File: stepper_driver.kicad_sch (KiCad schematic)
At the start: 7 parts, among them J20 StepperA, J21 StepperB, U3 TMC2208_SILENTSTEPSTICK

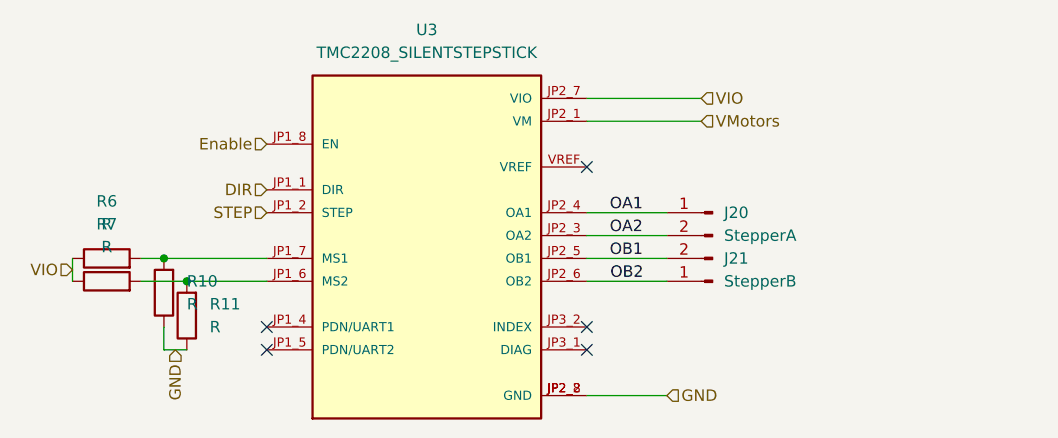
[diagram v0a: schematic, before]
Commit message: add second AX12 connector + change stepper connectors + add 12V connector. Todo : add SPI for RFID
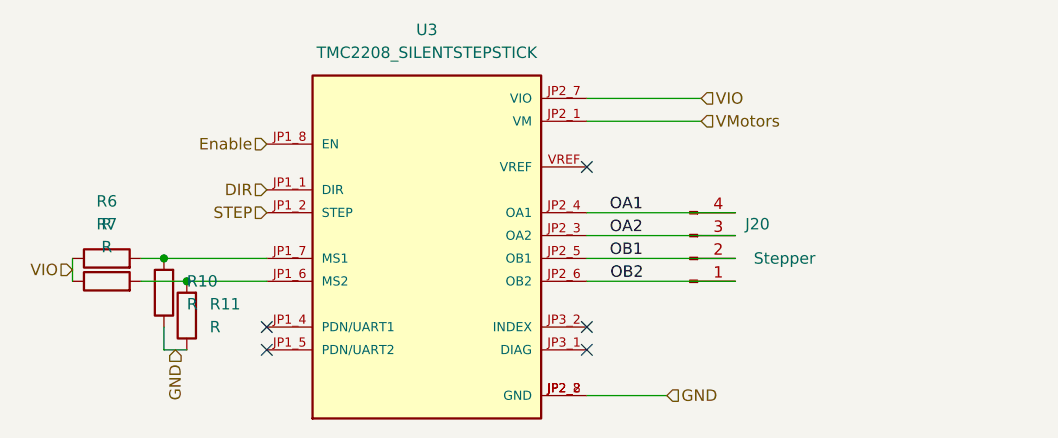
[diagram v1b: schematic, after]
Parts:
- removed J20: StepperA, Connector_Phoenix_MC:PhoenixContact_MC_1,5_2-G-3.81_1x02_P3.81mm_Horizontal, symbol Connector:Conn_01x02_Male
- removed J21: StepperB, Connector_Phoenix_MC:PhoenixContact_MC_1,5_2-G-3.81_1x02_P3.81mm_Horizontal, symbol Connector:Conn_01x02_Male
- added J20: Stepper, Connector_JST:JST_XH_B4B-XH-A_1x04_P2.50mm_Vertical, symbol Connector:Conn_01x04_Male
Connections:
- net OA1: now also J20.4 (Pin_4)
- net OA2: now also J20.3 (Pin_3)
- net OB1: now also J20.2 (Pin_2)
- net OB2: now also J20.1 (Pin_1)
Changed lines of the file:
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@@
   (no_connect (at 92.71 87.63))
   (no_connect (at 128.27 85.09))
-  (wire (pts (xy 137.16 72.39) (xy 128.27 72.39))
+  (wire (pts (xy 144.78 72.39) (xy 128.27 72.39))
     (stroke (width 0) (type default) (color 0 0 0 0))
   )
@@
     (stroke (width 0) (type default) (color 0 0 0 0))
   )
-  (wire (pts (xy 137.16 80.01) (xy 128.27 80.01))
+  (wire (pts (xy 144.78 80.01) (xy 128.27 80.01))
     (stroke (width 0) (type default) (color 0 0 0 0))
   )
@@
     (stroke (width 0) (type default) (color 0 0 0 0))
   )
-  (wire (pts (xy 137.16 77.47) (xy 128.27 77.47))
+  (wire (pts (xy 144.78 77.47) (xy 128.27 77.47))
     (stroke (width 0) (type default) (color 0 0 0 0))
   )
@@
     (stroke (width 0) (type default) (color 0 0 0 0))
   )
-  (wire (pts (xy 137.16 74.93) (xy 128.27 74.93))
+  (wire (pts (xy 144.78 74.93) (xy 128.27 74.93))
     (stroke (width 0) (type default) (color 0 0 0 0))
   )
@@
     (pin "1")
     (pin "2")
+  )
+  (symbol (lib_id "Connector:Conn_01x04_Male") (at 139.7 77.47 0) (mirror x) (unit 1)
+    (in_bom yes) (on_board yes)
+    (property "Reference" "J20" (id 0) (at 148.59 73.66 0)
+      (effects (font (size 1.27 1.27)) (justify right))
+    )
+    (property "Value" "Stepper" (id 1) (at 153.67 77.47 0)
+      (effects (font (size 1.27 1.27)) (justify right))
+    )
+    (property "Footprint" "Connector_JST:JST_XH_B4B-XH-A_1x04_P2.50mm_Vertical" (id 2) (at 139.7 77.47 0)
+      (effects (font (size 1.27 1.27)) hide)
+    )
+    (property "Datasheet" "~" (id 3) (at 139.7 77.47 0)
+      (effects (font (size 1.27 1.27)) hide)
+    )
+    (pin "1")
+    (pin "2")
+    (pin "3")
+    (pin "4")
   )
   (symbol (lib_id "TMC2208_SILENTSTEPSTICK:TMC2208_SILENTSTEPSTICK") (at 110.49 74.93 0) (unit 1)
@@
     (pin "VREF")
   )
-  (symbol (lib_id "Connector:Conn_01x02_Male") (at 142.24 80.01 180) (unit 1)
-    (in_bom yes) (on_board yes) (fields_autoplaced)
-    (property "Reference" "J21" (id 0) (at 143.51 77.4699 0)
-      (effects (font (size 1.27 1.27)) (justify right))
-    )
-    (property "Value" "StepperB" (id 1) (at 143.51 80.0099 0)
-      (effects (font (size 1.27 1.27)) (justify right))
-    )
-    (property "Footprint" "Connector_Phoenix_MC:PhoenixContact_MC_1,5_2-G-3.81_1x02_P3.81mm_Horizontal" (id 2) (at 142.24 80.01 0)
-      (effects (font (size 1.27 1.27)) hide)
-    )
-    (property "Datasheet" "~" (id 3) (at 142.24 80.01 0)
-      (effects (font (size 1.27 1.27)) hide)
-    )
-    (pin "1")
-    (pin "2")
-  )
   (symbol (lib_id "Device:R") (at 81.28 81.28 180) (unit 1)
     (in_bom yes) (on_board yes) (fields_autoplaced)
@@
       (effects (font (size 1.27 1.27)) hide)
     )
-    (pin "1")
-    (pin "2")
-  )
-  (symbol (lib_id "Connector:Conn_01x02_Male") (at 142.24 72.39 0) (mirror y) (unit 1)
-    (in_bom yes) (on_board yes) (fields_autoplaced)
-    (property "Reference" "J20" (id 0) (at 143.51 72.3899 0)
-      (effects (font (size 1.27 1.27)) (justify right))
-    )
-    (property "Value" "StepperA" (id 1) (at 143.51 74.9299 0)
-      (effects (font (size 1.27 1.27)) (justify right))
-    )
-    (property "Footprint" "Connector_Phoenix_MC:PhoenixContact_MC_1,5_2-G-3.81_1x02_P3.81mm_Horizontal" (id 2) (at 142.24 72.39 0)
-      (effects (font (size 1.27 1.27)) hide)
-    )
-    (property "Datasheet" "~" (id 3) (at 142.24 72.39 0)
-      (effects (font (size 1.27 1.27)) hide)
-    )

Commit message: Add SPI connector + route control pins (LEDs, AX12)
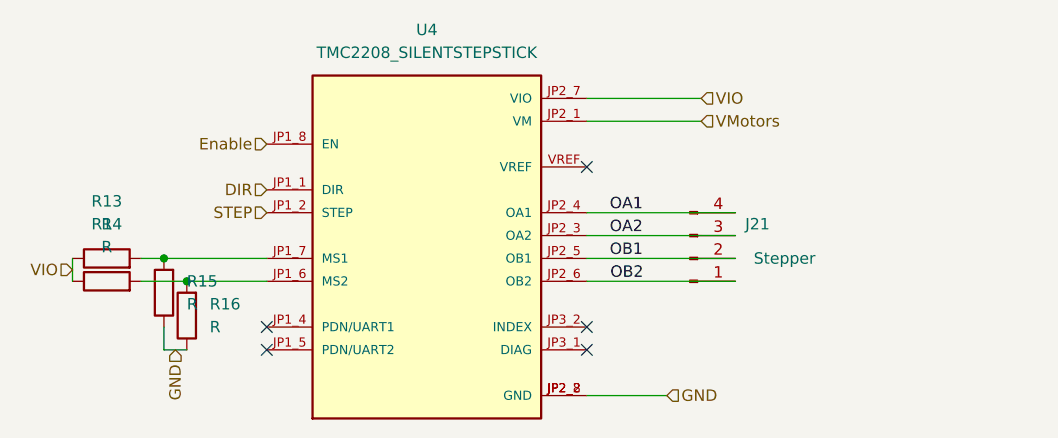
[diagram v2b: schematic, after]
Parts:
- renumbered J20 to J21, R6 to R13, R7 to R14, R10 to R15, R11 to R16, U3 to U4
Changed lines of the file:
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@@
     (effects (font (size 1.27 1.27)) (justify left))
   )
-  (symbol (lib_id "Device:R") (at 74.93 80.01 90) (unit 1)
+  (symbol (lib_id "Device:R") (at 74.93 80.01 90)
     (in_bom yes) (on_board yes) (fields_autoplaced)
-    (property "Reference" "R7" (id 0) (at 74.93 73.66 90))
+    (property "Reference" "R14" (id 0) (at 74.93 73.66 90))
     (property "Value" "R" (id 1) (at 74.93 76.2 90))
     (property "Footprint" "Resistor_SMD:R_0603_1608Metric" (id 2) (at 74.93 81.788 90)
@@
     (pin "2")
   )
-  (symbol (lib_id "Device:R") (at 83.82 83.82 180) (unit 1)
+  (symbol (lib_id "Device:R") (at 83.82 83.82 180)
     (in_bom yes) (on_board yes) (fields_autoplaced)
-    (property "Reference" "R11" (id 0) (at 86.36 82.5499 0)
+    (property "Reference" "R16" (id 0) (at 86.36 82.5499 0)
       (effects (font (size 1.27 1.27)) (justify right))
     )
@@
     (pin "2")
   )
-  (symbol (lib_id "Connector:Conn_01x04_Male") (at 139.7 77.47 0) (mirror x) (unit 1)
+  (symbol (lib_id "Connector:Conn_01x04_Male") (at 139.7 77.47 0) (mirror x)
     (in_bom yes) (on_board yes)
-    (property "Reference" "J20" (id 0) (at 148.59 73.66 0)
+    (property "Reference" "J21" (id 0) (at 148.59 73.66 0)
       (effects (font (size 1.27 1.27)) (justify right))
     )
@@
     (pin "4")
   )
-  (symbol (lib_id "TMC2208_SILENTSTEPSTICK:TMC2208_SILENTSTEPSTICK") (at 110.49 74.93 0) (unit 1)
+  (symbol (lib_id "TMC2208_SILENTSTEPSTICK:TMC2208_SILENTSTEPSTICK") (at 110.49 74.93 0)
     (in_bom yes) (on_board yes) (fields_autoplaced)
-    (property "Reference" "U3" (id 0) (at 110.49 52.07 0))
+    (property "Reference" "U4" (id 0) (at 110.49 52.07 0))
     (property "Value" "TMC2208_SILENTSTEPSTICK" (id 1) (at 110.49 54.61 0))
     (property "Footprint" "TMC2208_SILENTSTEPSTICK:MODULE_TMC2208_SILENTSTEPSTICK" (id 2) (at 110.49 74.93 0)
@@
     (pin "VREF")
   )
-  (symbol (lib_id "Device:R") (at 81.28 81.28 180) (unit 1)
+  (symbol (lib_id "Device:R") (at 81.28 81.28 180)
     (in_bom yes) (on_board yes) (fields_autoplaced)
-    (property "Reference" "R10" (id 0) (at 83.82 80.0099 0)
+    (property "Reference" "R15" (id 0) (at 83.82 80.0099 0)
       (effects (font (size 1.27 1.27)) (justify right))
     )
@@
     (pin "2")
   )
-  (symbol (lib_id "Device:R") (at 74.93 77.47 90) (unit 1)
+  (symbol (lib_id "Device:R") (at 74.93 77.47 90)
     (in_bom yes) (on_board yes) (fields_autoplaced)
-    (property "Reference" "R6" (id 0) (at 74.93 71.12 90))
+    (property "Reference" "R13" (id 0) (at 74.93 71.12 90))
     (property "Value" "R" (id 1) (at 74.93 73.66 90))
     (property "Footprint" "Resistor_SMD:R_0603_1608Metric" (id 2) (at 74.93 79.248 90)

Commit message: add zeners for new connections
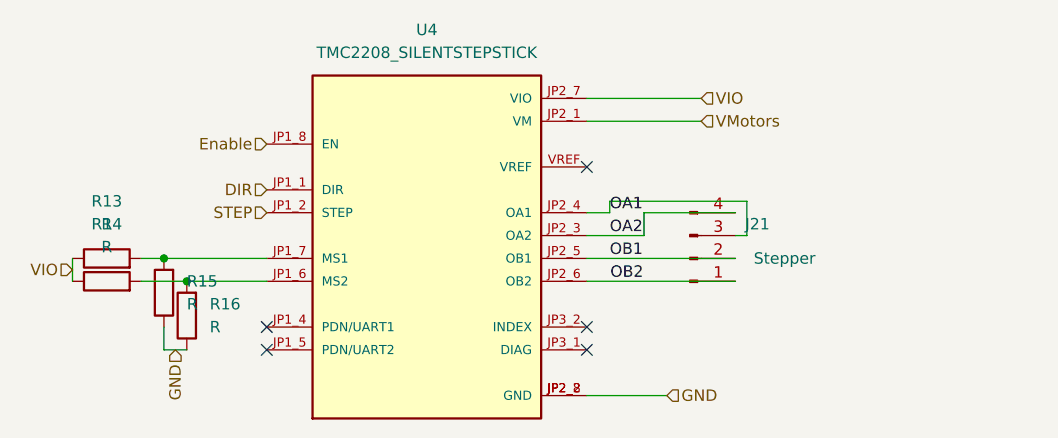
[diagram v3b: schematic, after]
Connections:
- net OA1: now also J21.3 (Pin_3); no longer J21.4 (Pin_4)
- net OA2: now also J21.4 (Pin_4); no longer J21.3 (Pin_3)
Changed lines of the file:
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@@
   (no_connect (at 92.71 87.63))
   (no_connect (at 128.27 85.09))
-  (wire (pts (xy 144.78 72.39) (xy 128.27 72.39))
-    (stroke (width 0) (type default) (color 0 0 0 0))
-  )
   (wire (pts (xy 137.16 92.71) (xy 128.27 92.71))
     (stroke (width 0) (type default) (color 0 0 0 0))
@@
     (stroke (width 0) (type default) (color 0 0 0 0))
   )
+  (wire (pts (xy 128.27 74.93) (xy 134.62 74.93))
+    (stroke (width 0) (type default) (color 0 0 0 0))
+  )
   (wire (pts (xy 78.74 80.01) (xy 83.82 80.01))
+    (stroke (width 0) (type default) (color 0 0 0 0))
+  )
+  (wire (pts (xy 128.27 72.39) (xy 130.81 72.39))
+    (stroke (width 0) (type default) (color 0 0 0 0))
+  )
+  (wire (pts (xy 134.62 72.39) (xy 144.78 72.39))
     (stroke (width 0) (type default) (color 0 0 0 0))
   )
@@
     (stroke (width 0) (type default) (color 0 0 0 0))
   )
+  (wire (pts (xy 146.05 74.93) (xy 144.78 74.93))
+    (stroke (width 0) (type default) (color 0 0 0 0))
+  )
   (wire (pts (xy 81.28 87.63) (xy 81.28 85.09))
+    (stroke (width 0) (type default) (color 0 0 0 0))
+  )
+  (wire (pts (xy 130.81 72.39) (xy 130.81 71.12))
     (stroke (width 0) (type default) (color 0 0 0 0))
   )
@@
     (stroke (width 0) (type default) (color 0 0 0 0))
   )
+  (wire (pts (xy 146.05 71.12) (xy 146.05 74.93))
+    (stroke (width 0) (type default) (color 0 0 0 0))
+  )
+  (wire (pts (xy 134.62 74.93) (xy 134.62 72.39))
+    (stroke (width 0) (type default) (color 0 0 0 0))
+  )
   (wire (pts (xy 81.28 77.47) (xy 92.71 77.47))
     (stroke (width 0) (type default) (color 0 0 0 0))
@@
     (stroke (width 0) (type default) (color 0 0 0 0))
   )
-  (wire (pts (xy 144.78 74.93) (xy 128.27 74.93))
+  (wire (pts (xy 130.81 71.12) (xy 146.05 71.12))
     (stroke (width 0) (type default) (color 0 0 0 0))
   )

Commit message: route STEP and DIR for both stepper motors
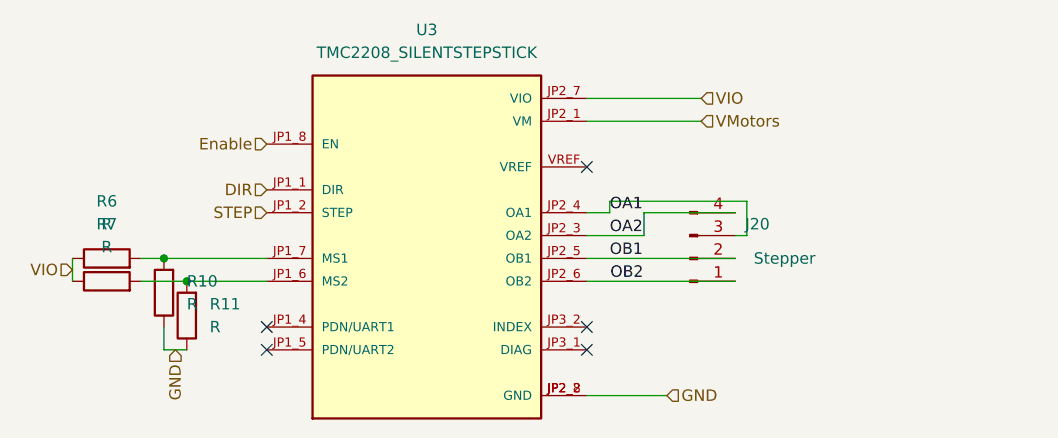
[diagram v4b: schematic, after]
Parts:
- renumbered J21 to J20, R15 to R10, R16 to R11, R13 to R6, R14 to R7, U4 to U3
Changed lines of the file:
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@@
     (effects (font (size 1.27 1.27)) (justify left))
   )
-  (symbol (lib_id "Device:R") (at 74.93 80.01 90)
+  (symbol (lib_id "Device:R") (at 74.93 80.01 90) (unit 1)
     (in_bom yes) (on_board yes) (fields_autoplaced)
-    (property "Reference" "R14" (id 0) (at 74.93 73.66 90))
+    (property "Reference" "R7" (id 0) (at 74.93 73.66 90))
     (property "Value" "R" (id 1) (at 74.93 76.2 90))
     (property "Footprint" "Resistor_SMD:R_0603_1608Metric" (id 2) (at 74.93 81.788 90)
@@
     (pin "2")
   )
-  (symbol (lib_id "Device:R") (at 83.82 83.82 180)
+  (symbol (lib_id "Device:R") (at 83.82 83.82 180) (unit 1)
     (in_bom yes) (on_board yes) (fields_autoplaced)
-    (property "Reference" "R16" (id 0) (at 86.36 82.5499 0)
+    (property "Reference" "R11" (id 0) (at 86.36 82.5499 0)
       (effects (font (size 1.27 1.27)) (justify right))
     )
@@
     (pin "2")
   )
-  (symbol (lib_id "Connector:Conn_01x04_Male") (at 139.7 77.47 0) (mirror x)
+  (symbol (lib_id "Connector:Conn_01x04_Male") (at 139.7 77.47 0) (mirror x) (unit 1)
     (in_bom yes) (on_board yes)
-    (property "Reference" "J21" (id 0) (at 148.59 73.66 0)
+    (property "Reference" "J20" (id 0) (at 148.59 73.66 0)
       (effects (font (size 1.27 1.27)) (justify right))
     )
@@
     (pin "4")
   )
-  (symbol (lib_id "TMC2208_SILENTSTEPSTICK:TMC2208_SILENTSTEPSTICK") (at 110.49 74.93 0)
+  (symbol (lib_id "TMC2208_SILENTSTEPSTICK:TMC2208_SILENTSTEPSTICK") (at 110.49 74.93 0) (unit 1)
     (in_bom yes) (on_board yes) (fields_autoplaced)
-    (property "Reference" "U4" (id 0) (at 110.49 52.07 0))
+    (property "Reference" "U3" (id 0) (at 110.49 52.07 0))
     (property "Value" "TMC2208_SILENTSTEPSTICK" (id 1) (at 110.49 54.61 0))
     (property "Footprint" "TMC2208_SILENTSTEPSTICK:MODULE_TMC2208_SILENTSTEPSTICK" (id 2) (at 110.49 74.93 0)
@@
     (pin "VREF")
   )
-  (symbol (lib_id "Device:R") (at 81.28 81.28 180)
+  (symbol (lib_id "Device:R") (at 81.28 81.28 180) (unit 1)
     (in_bom yes) (on_board yes) (fields_autoplaced)
-    (property "Reference" "R15" (id 0) (at 83.82 80.0099 0)
+    (property "Reference" "R10" (id 0) (at 83.82 80.0099 0)
       (effects (font (size 1.27 1.27)) (justify right))
     )
@@
     (pin "2")
   )
-  (symbol (lib_id "Device:R") (at 74.93 77.47 90)
+  (symbol (lib_id "Device:R") (at 74.93 77.47 90) (unit 1)
     (in_bom yes) (on_board yes) (fields_autoplaced)
-    (property "Reference" "R13" (id 0) (at 74.93 71.12 90))
+    (property "Reference" "R6" (id 0) (at 74.93 71.12 90))
     (property "Value" "R" (id 1) (at 74.93 73.66 90))
     (property "Footprint" "Resistor_SMD:R_0603_1608Metric" (id 2) (at 74.93 79.248 90)

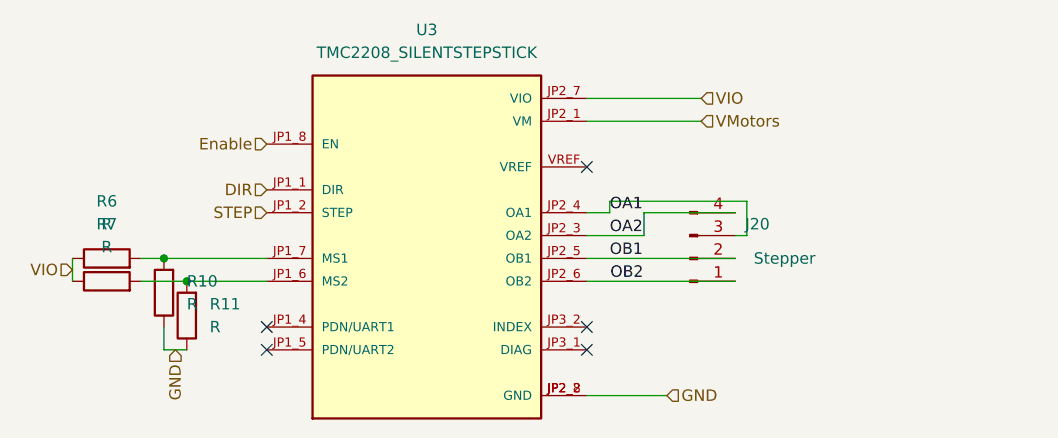
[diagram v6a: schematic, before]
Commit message: fix warnings + separate enable for Steppers
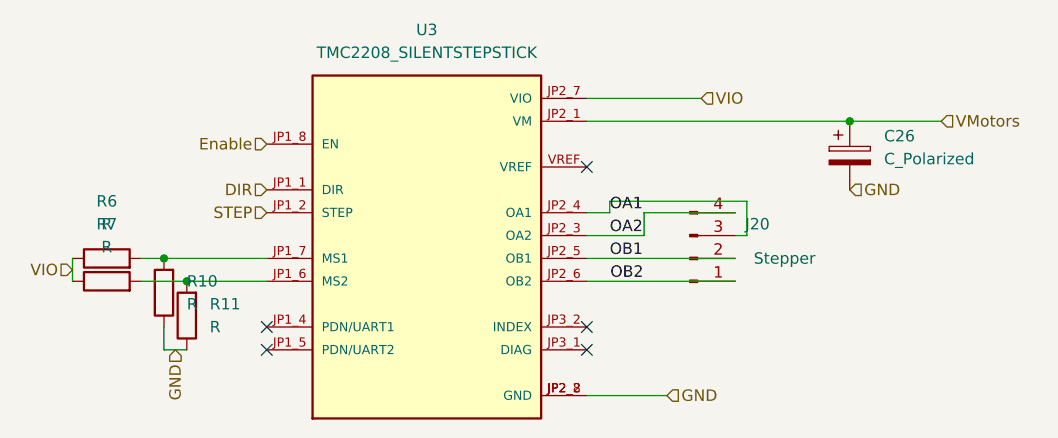
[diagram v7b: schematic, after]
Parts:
- added C26: C_Polarized, Capacitor_THT:CP_Radial_D10.0mm_P5.00mm, symbol Device:C_Polarized
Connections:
- net GND: now also C26.2
- net VMotors: now also C26.1
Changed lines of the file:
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@@
 	(paper "A4")
+	(junction
+		(at 157.48 62.23)
+		(diameter 0)
+		(color 0 0 0 0)
+	)
 	(junction
 		(at 81.28 77.47)
@@
 	(wire
 		(pts
+			(xy 157.48 62.23) (xy 167.64 62.23)
+		)
+		(stroke
+			(width 0)
+			(type default)
+		)
+	)
+	(wire
+		(pts
 			(xy 78.74 77.47) (xy 81.28 77.47)
 		)
@@
 	(wire
 		(pts
-			(xy 128.27 62.23) (xy 140.97 62.23)
+			(xy 128.27 62.23) (xy 157.48 62.23)
 		)
 		(stroke
@@
 		)
 	)
+	(hierarchical_label "GND"
+		(shape input)
+		(at 157.48 69.85 0)
+		(effects
+			(font
+				(size 1.27 1.27)
+			)
+			(justify left)
+		)
+	)
 	(hierarchical_label "Enable"
 		(shape input)
@@
 	(hierarchical_label "VMotors"
 		(shape input)
-		(at 140.97 62.23 0)
+		(at 167.64 62.23 0)
 		(effects
 			(font
@@
 		)
 	)
+	(symbol
+		(lib_id "Device:C_Polarized")
+		(at 157.48 66.04 0)
+		(unit 1)
+		(exclude_from_sim no)
+		(in_bom yes)
+		(on_board yes)
+		(dnp no)
+		(fields_autoplaced yes)
+		(property "Reference" "C26"
+			(at 161.29 63.8809 0)
+			(effects
+				(font
+					(size 1.27 1.27)
+				)
+				(justify left)
+			)
+		)
+		(property "Value" "C_Polarized"
+			(at 161.29 66.4209 0)
+			(effects
+				(font
+					(size 1.27 1.27)
+				)
+				(justify left)
+			)
+		)
+		(property "Footprint" "Capacitor_THT:CP_Radial_D10.0mm_P5.00mm"
+			(at 158.4452 69.85 0)
+			(effects
+				(font
+					(size 1.27 1.27)
+				)
+				(hide yes)
+			)
+		)
+		(property "Datasheet" "~"
+			(at 157.48 66.04 0)
+			(effects
+				(font
+					(size 1.27 1.27)
+				)
+				(hide yes)
+			)
+		)
+		(property "Description" ""
+			(at 157.48 66.04 0)
+			(effects
+				(font
+					(size 1.27 1.27)
+				)
+				(hide yes)
+			)
+		)
+		(pin "1"
+		)
+		(pin "2"
+		)
+		(instances
+			(project "carte_servo"
+				(path "/e63e39d7-6ac0-4ffd-8aa3-1841a4541b55/4bdf100d-7e35-4013-89a2-8f86fd135421"
+					(reference "C26")
+					(unit 1)
+				)
+				(path "/e63e39d7-6ac0-4ffd-8aa3-1841a4541b55/f86a3d70-fa31-4725-b330-81e2f5dad2cc"
+					(reference "C27")
+					(unit 1)
+				)
+			)
+		)
+	)
